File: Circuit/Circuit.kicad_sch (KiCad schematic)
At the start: 7 parts, among them U1 A1302KUA-T, U2 L293, U3 MODEL 3, U4 MODEL #

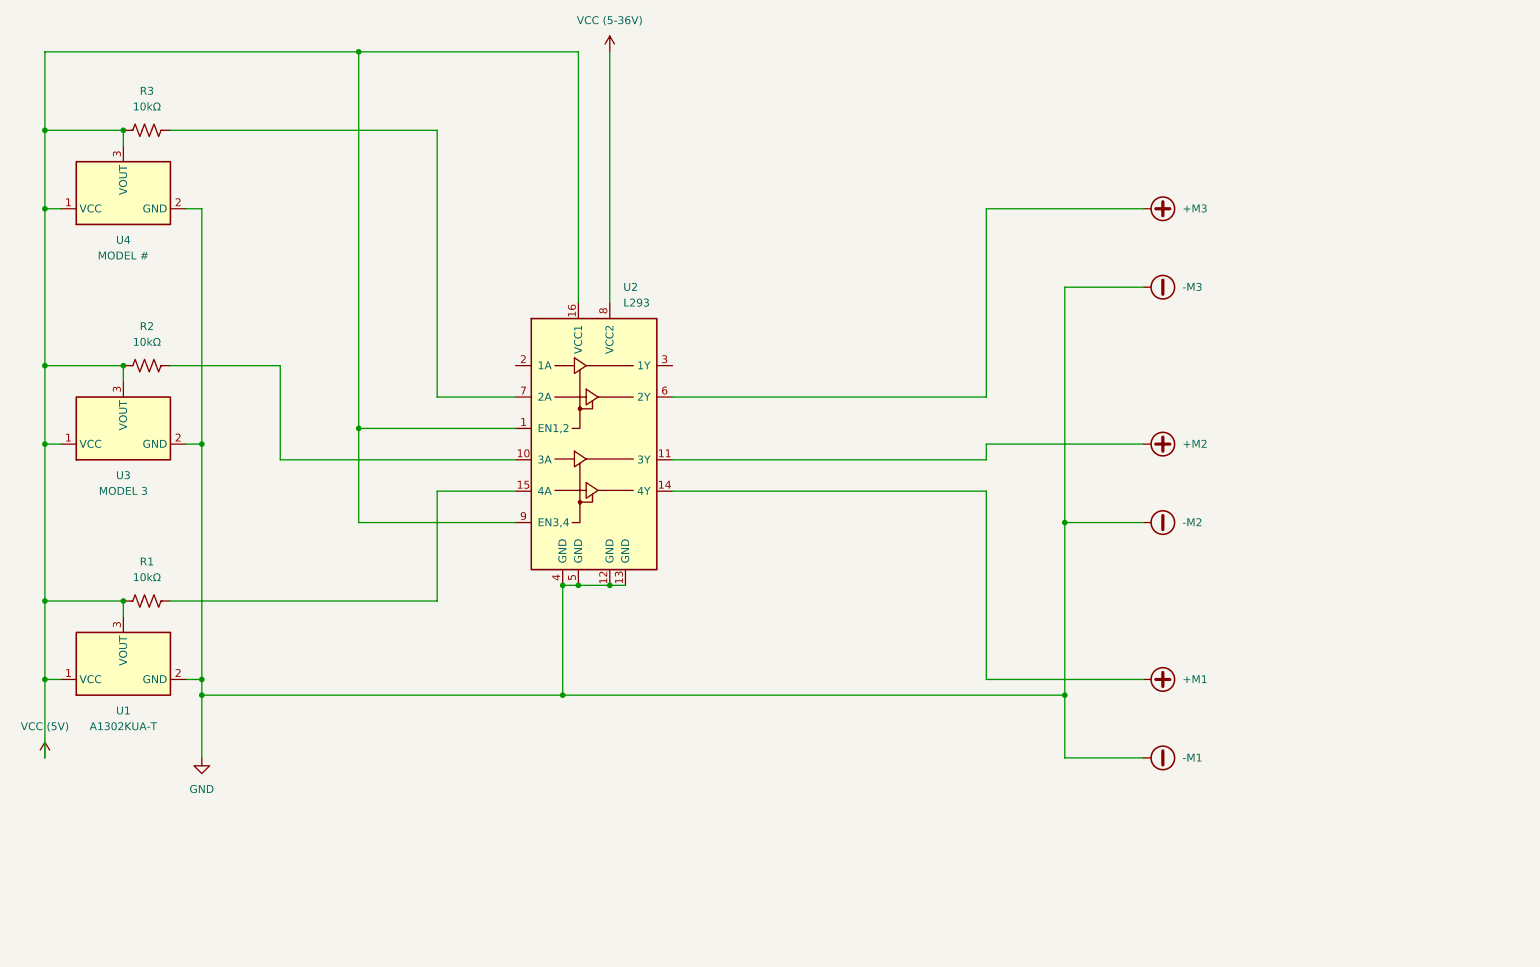
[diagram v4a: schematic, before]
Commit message: Added H-Bridges and Inverters for N/S switching emags
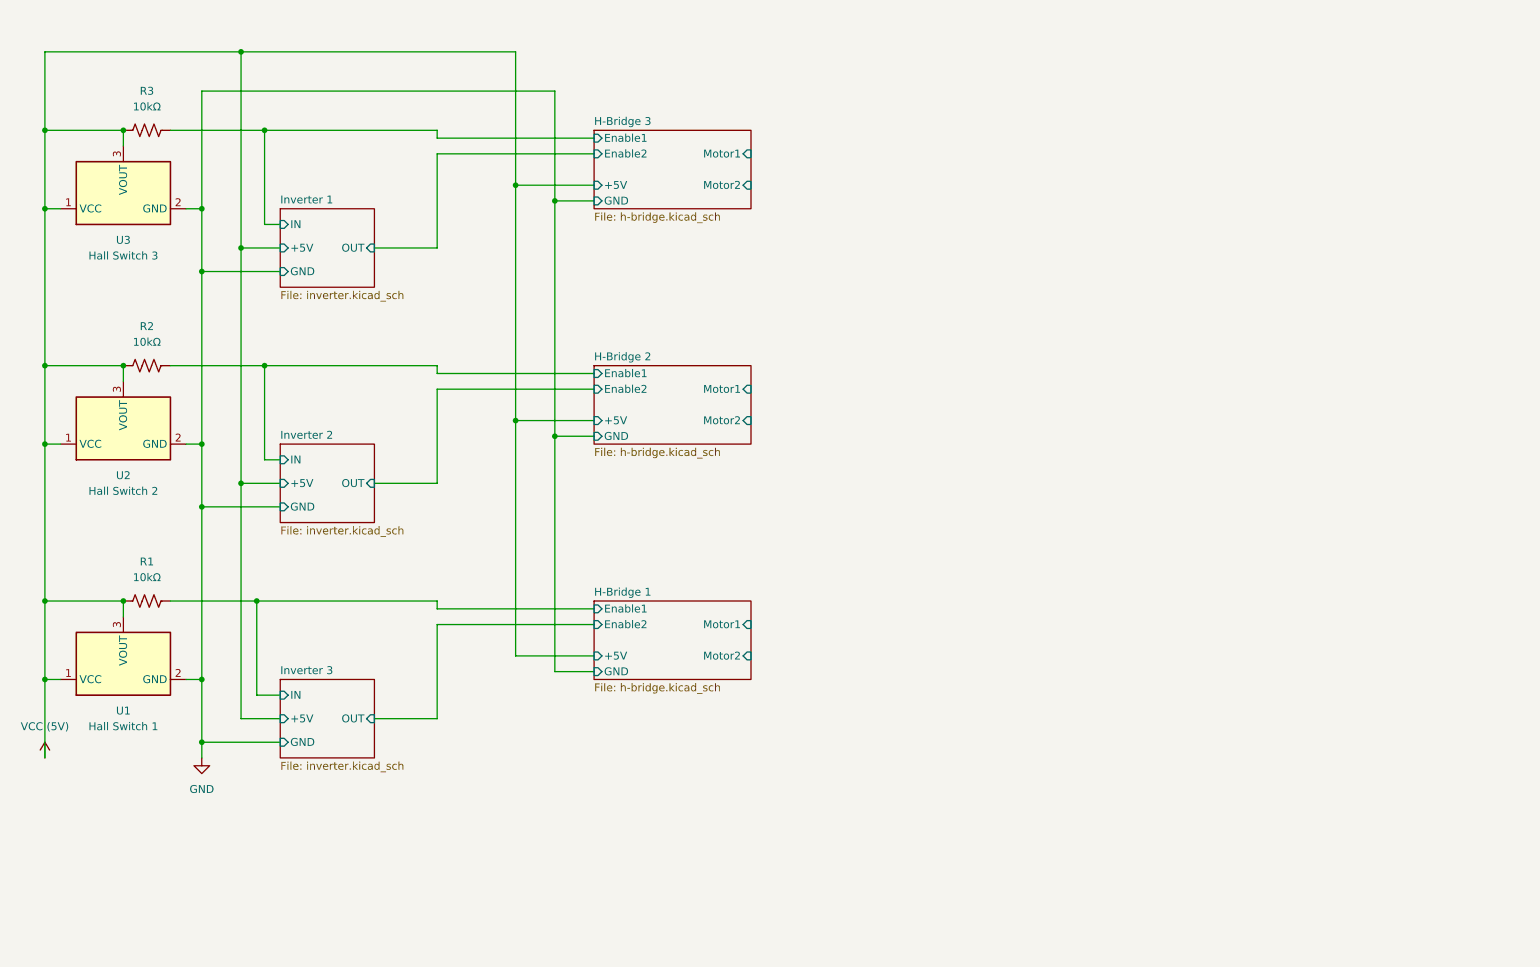
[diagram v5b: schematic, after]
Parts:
- removed U2: L293, Package_DIP:DIP-16_W7.62mm, symbol Driver_Motor:L293
- U1: value A1302KUA-T -> Hall Switch 1
- U2: renamed from U3; value MODEL 3 -> Hall Switch 2
- U3: renamed from U4; value MODEL # -> Hall Switch 3
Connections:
- net H-Bridge 2/Enable1: now reaches R2.2
- net H-Bridge 1/Enable1: now reaches R1.2
- net H-Bridge 3/Enable1: now reaches R3.2
- net -M1 renamed GND
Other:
- added sheet H-Bridge 1 (h-bridge.kicad_sch)
- added sheet H-Bridge 2 (h-bridge.kicad_sch)
- added sheet H-Bridge 3 (h-bridge.kicad_sch)
- added sheet Inverter 1 (inverter.kicad_sch)
- added sheet Inverter 2 (inverter.kicad_sch)
- added sheet Inverter 3 (inverter.kicad_sch)

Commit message: Added support for 2 power supplies (5V and 0-30V) and used mosfets
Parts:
- added L1: EMAG3, symbol Device:L
- added L2: EMAG2, symbol Device:L
- added L3: EMAG1, symbol Device:L
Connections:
- new net H-Bridge 1/Emag1: L3.1
- new net H-Bridge 1/Emag2: L3.2
- new net H-Bridge 2/Emag1: L2.1
- new net H-Bridge 2/Emag2: L2.2
- new net H-Bridge 3/Emag1: L1.1
- new net H-Bridge 3/Emag2: L1.2
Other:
- sheet H-Bridge 1 ports: added Emag1, Emag2, Vcc; removed Motor1, Motor2
- sheet H-Bridge 2 ports: added Emag1, Emag2, Vcc; removed Motor1, Motor2
- sheet H-Bridge 3 ports: added Emag1, Emag2, Vcc; removed Motor1, Motor2
